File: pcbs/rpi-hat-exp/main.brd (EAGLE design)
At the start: 65 x 56 mm, 16 parts, among them IC1 MCP23017, IC2 L293D, J2 1X2-3.5MM, J3 1X2-3.5MM, U1 MCP3002

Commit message: I changed 'some' stuff
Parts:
- removed LED1: RGBLED_CA-5MM, adafruit:LED5MMRGB
- removed R1: 220, adafruit:0204/7
- removed R2: 330, adafruit:0204/7
- added LED2: WS2812BTH, adafruit:LED5MMRGB
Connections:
- removed net GPIO13M: LED1.1, R1.1, R2.2
- new net GPIO18: JP2.12, LED2.1
- net GND: now also LED2.3; no longer LED1.2, R2.1
- net GPIO05: no longer LED1.4
- net GPIO06: no longer LED1.3
- net GPIO13: no longer R1.2
- net VCC: now also LED2.2
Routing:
- net GPIO18: track 0.00 -> 47.4 mm
- net GPIO05: track 34.1 -> 0.00 mm
- net GPIO06: track 17.5 -> 0.00 mm
- net GPIO13: track 7.18 -> 0.00 mm
- net GPIO13M: track 6.13 -> 0.00 mm
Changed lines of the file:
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@@
 <setting verticaltext="up"/>
 </settings>
-<grid distance="0.05" unitdist="inch" unit="inch" style="lines" multiple="1" display="no" altdistance="0.025" altunitdist="inch" altunit="inch"/>
+<grid distance="0.05" unitdist="inch" unit="inch" style="lines" multiple="1" display="no" altdistance="0.0125" altunitdist="inch" altunit="inch"/>
 <layers>
 <layer number="1" name="Top" color="4" fill="1" visible="yes" active="yes"/>
@@
 <attribute name="VALUE" x="7.366" y="48.0314" size="1.27" layer="27"/>
 </element>
-<element name="LED1" library="adafruit" package="LED5MMRGB" value="RGBLED_CA-5MM" x="60.96" y="45.085" smashed="yes">
-<attribute name="NAME" x="59.69" y="40.005" size="1.27" layer="21"/>
-</element>
-<element name="R1" library="adafruit" package="0204/7" value="220" x="52.07" y="44.45" smashed="yes" rot="R180">
-<attribute name="NAME" x="51.435" y="46.9646" size="0.9906" layer="25" ratio="12" rot="R180"/>
-<attribute name="VALUE" x="51.0794" y="43.9674" size="0.8128" layer="21" ratio="12"/>
-</element>
-<element name="R2" library="adafruit" package="0204/7" value="330" x="52.07" y="41.91" smashed="yes">
-<attribute name="NAME" x="53.34" y="39.3954" size="0.9906" layer="25" ratio="12"/>
-<attribute name="VALUE" x="51.0794" y="41.4274" size="0.8128" layer="21" ratio="12"/>
-</element>
+<element name="LED2" library="adafruit" package="LED5MMRGB" value="WS2812BTH" x="59.69" y="44.45" rot="R270"/>
 </elements>
 <signals>
@@
 <contactref element="JP2" pad="14"/>
 <contactref element="JP2" pad="6"/>
-<contactref element="LED1" pad="2"/>
-<contactref element="R2" pad="1"/>
 <polygon width="0.4064" layer="16">
 <vertex x="0" y="55.88"/>
@@
 <vertex x="64.77" y="55.88"/>
 </polygon>
+<contactref element="LED2" pad="3"/>
 </signal>
 <signal name="VCC">
@@
 <vertex x="-1.27" y="0"/>
 </polygon>
+<contactref element="LED2" pad="2"/>
 </signal>
 <signal name="5V">
@@
 <signal name="GPIO13">
 <contactref element="JP2" pad="33"/>
-<contactref element="R1" pad="2"/>
-<wire x1="48.26" y1="44.45" x2="49.276" y2="45.466" width="0.4064" layer="1"/>
-<wire x1="49.276" y1="45.466" x2="49.276" y2="51.2064" width="0.4064" layer="1"/>
 </signal>
 <signal name="N$1">
@@
 <signal name="GPIO06">
 <contactref element="JP2" pad="31"/>
-<contactref element="LED1" pad="3"/>
-<wire x1="61.849" y1="46.0534" x2="59.6424" y2="48.26" width="0.4064" layer="16"/>
-<wire x1="59.6424" y1="48.26" x2="49.1744" y2="48.26" width="0.4064" layer="16"/>
-<wire x1="49.1744" y1="48.26" x2="46.736" y2="50.6984" width="0.4064" layer="16"/>
-<wire x1="46.736" y1="50.6984" x2="46.736" y2="51.2064" width="0.4064" layer="16"/>
 </signal>
 <signal name="GPIO05">
 <contactref element="JP2" pad="29"/>
-<contactref element="LED1" pad="4"/>
-<wire x1="63.119" y1="44.1166" x2="63.119" y2="40.259" width="0.4064" layer="16"/>
-<wire x1="63.119" y1="40.259" x2="62.23" y2="39.37" width="0.4064" layer="16"/>
-<wire x1="45.72" y1="39.37" x2="62.23" y2="39.37" width="0.4064" layer="16"/>
-<wire x1="44.196" y1="51.2064" x2="44.196" y2="40.894" width="0.4064" layer="16"/>
-<wire x1="44.196" y1="40.894" x2="45.72" y2="39.37" width="0.4064" layer="16"/>
-</signal>
-<signal name="GPIO13M">
-<contactref element="LED1" pad="1"/>
-<contactref element="R1" pad="1"/>
-<contactref element="R2" pad="2"/>
-<wire x1="55.88" y1="41.91" x2="55.88" y2="44.45" width="0.4064" layer="1"/>
-<wire x1="55.88" y1="44.45" x2="57.4834" y2="46.0534" width="0.4064" layer="1"/>
-<wire x1="57.4834" y1="46.0534" x2="58.801" y2="46.0534" width="0.4064" layer="1"/>
+</signal>
+<signal name="GPIO18">
+<contactref element="JP2" pad="12"/>
+<contactref element="LED2" pad="1"/>
+<wire x1="60.6584" y1="46.609" x2="59.1185" y2="46.609" width="0.4064" layer="1"/>
+<wire x1="59.1185" y1="46.609" x2="58.1025" y2="47.625" width="0.4064" layer="1"/>
+<wire x1="58.1025" y1="47.625" x2="58.1025" y2="54.2925" width="0.4064" layer="1"/>
+<wire x1="58.1025" y1="54.2925" x2="57.15" y2="55.245" width="0.4064" layer="1"/>
+<wire x1="57.15" y1="55.245" x2="22.8346" y2="55.245" width="0.4064" layer="1"/>
+<wire x1="22.8346" y1="55.245" x2="21.336" y2="53.7464" width="0.4064" layer="1"/>
 </signal>
 </signals>

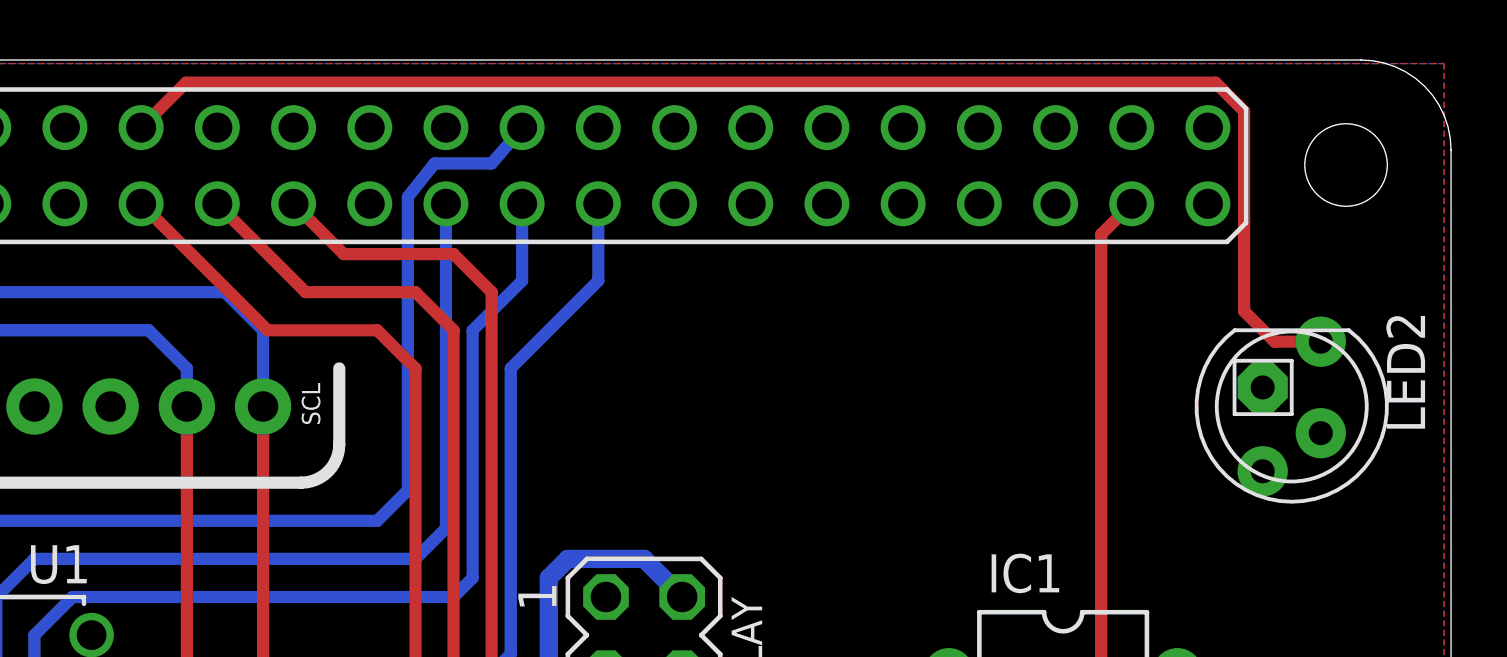
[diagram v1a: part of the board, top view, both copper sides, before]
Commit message: pump change wuhu $ board finalised
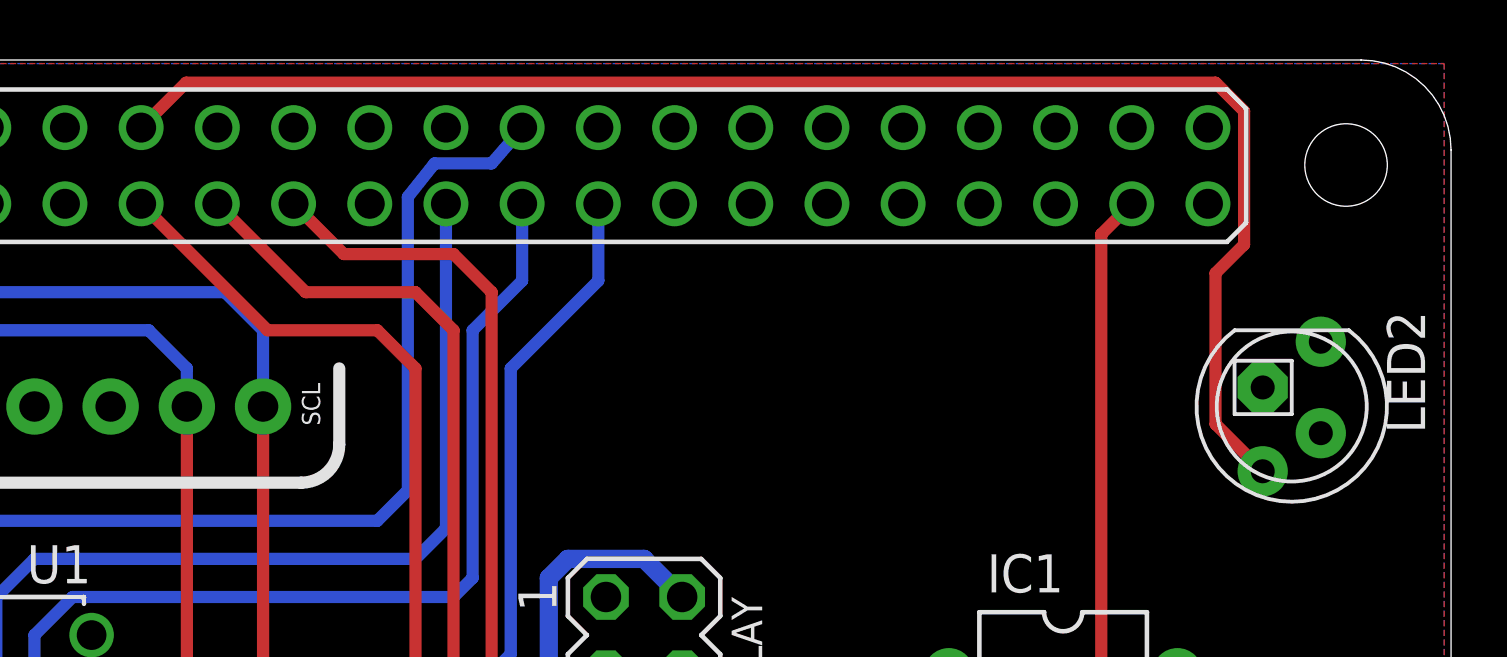
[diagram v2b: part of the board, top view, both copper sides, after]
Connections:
- net GND: now also LED2.2; no longer LED2.3
- net GPIO18: now also LED2.4; no longer LED2.1
- net VCC: now also LED2.3; no longer LED2.2
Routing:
- net GPIO18: track 47.4 -> 50.8 mm
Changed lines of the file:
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@@
 <?xml version="1.0" encoding="utf-8"?>
 <!DOCTYPE eagle SYSTEM "eagle.dtd">
-<eagle version="8.0.2">
+<eagle version="8.1.0">
 <drawing>
 <settings>
@@
 <layers>
 <layer number="1" name="Top" color="4" fill="1" visible="yes" active="yes"/>
+<layer number="2" name="Route2" color="1" fill="3" visible="no" active="yes"/>
+<layer number="3" name="Route3" color="4" fill="3" visible="no" active="yes"/>
+<layer number="4" name="Route4" color="1" fill="4" visible="no" active="yes"/>
+<layer number="5" name="Route5" color="4" fill="4" visible="no" active="yes"/>
+<layer number="6" name="Route6" color="1" fill="8" visible="no" active="yes"/>
+<layer number="7" name="Route7" color="4" fill="8" visible="no" active="yes"/>
+<layer number="8" name="Route8" color="1" fill="2" visible="no" active="yes"/>
+<layer number="9" name="Route9" color="4" fill="2" visible="no" active="yes"/>
+<layer number="10" name="Route10" color="1" fill="7" visible="no" active="yes"/>
+<layer number="11" name="Route11" color="4" fill="7" visible="no" active="yes"/>
+<layer number="12" name="Route12" color="1" fill="5" visible="no" active="yes"/>
+<layer number="13" name="Route13" color="4" fill="5" visible="no" active="yes"/>
+<layer number="14" name="Route14" color="1" fill="6" visible="no" active="yes"/>
+<layer number="15" name="Route15" color="4" fill="6" visible="no" active="yes"/>
 <layer number="16" name="Bottom" color="1" fill="1" visible="yes" active="yes"/>
 <layer number="17" name="Pads" color="2" fill="1" visible="yes" active="yes"/>
@@
 <vertex x="64.77" y="55.88"/>
 </polygon>
-<contactref element="LED2" pad="3"/>
+<contactref element="LED2" pad="2"/>
 </signal>
 <signal name="VCC">
@@
 <vertex x="-1.27" y="0"/>
 </polygon>
-<contactref element="LED2" pad="2"/>
+<contactref element="LED2" pad="3"/>
 </signal>
 <signal name="5V">
@@
 <signal name="GPIO18">
 <contactref element="JP2" pad="12"/>
-<contactref element="LED2" pad="1"/>
-<wire x1="60.6584" y1="46.609" x2="59.1185" y2="46.609" width="0.4064" layer="1"/>
-<wire x1="59.1185" y1="46.609" x2="58.1025" y2="47.625" width="0.4064" layer="1"/>
-<wire x1="58.1025" y1="47.625" x2="58.1025" y2="54.2925" width="0.4064" layer="1"/>
-<wire x1="58.1025" y1="54.2925" x2="57.15" y2="55.245" width="0.4064" layer="1"/>
-<wire x1="57.15" y1="55.245" x2="22.8346" y2="55.245" width="0.4064" layer="1"/>
+<contactref element="LED2" pad="4"/>
+<wire x1="22.8346" y1="55.245" x2="57.15" y2="55.245" width="0.4064" layer="1"/>
 <wire x1="22.8346" y1="55.245" x2="21.336" y2="53.7464" width="0.4064" layer="1"/>
+<wire x1="57.15" y1="55.245" x2="58.1025" y2="54.2925" width="0.4064" layer="1"/>
+<wire x1="58.1025" y1="54.2925" x2="58.1025" y2="49.8475" width="0.4064" layer="1"/>
+<wire x1="58.1025" y1="49.8475" x2="57.15" y2="48.895" width="0.4064" layer="1"/>
+<wire x1="57.15" y1="43.8626" x2="58.7216" y2="42.291" width="0.4064" layer="1"/>
+<wire x1="57.15" y1="48.895" x2="57.15" y2="43.8626" width="0.4064" layer="1"/>
 </signal>
 </signals>
